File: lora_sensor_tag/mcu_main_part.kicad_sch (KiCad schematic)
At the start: 10 parts, among them U5 ESP32-WROOM-32D, U6 SHT20, U7 SX1276IMLTRT

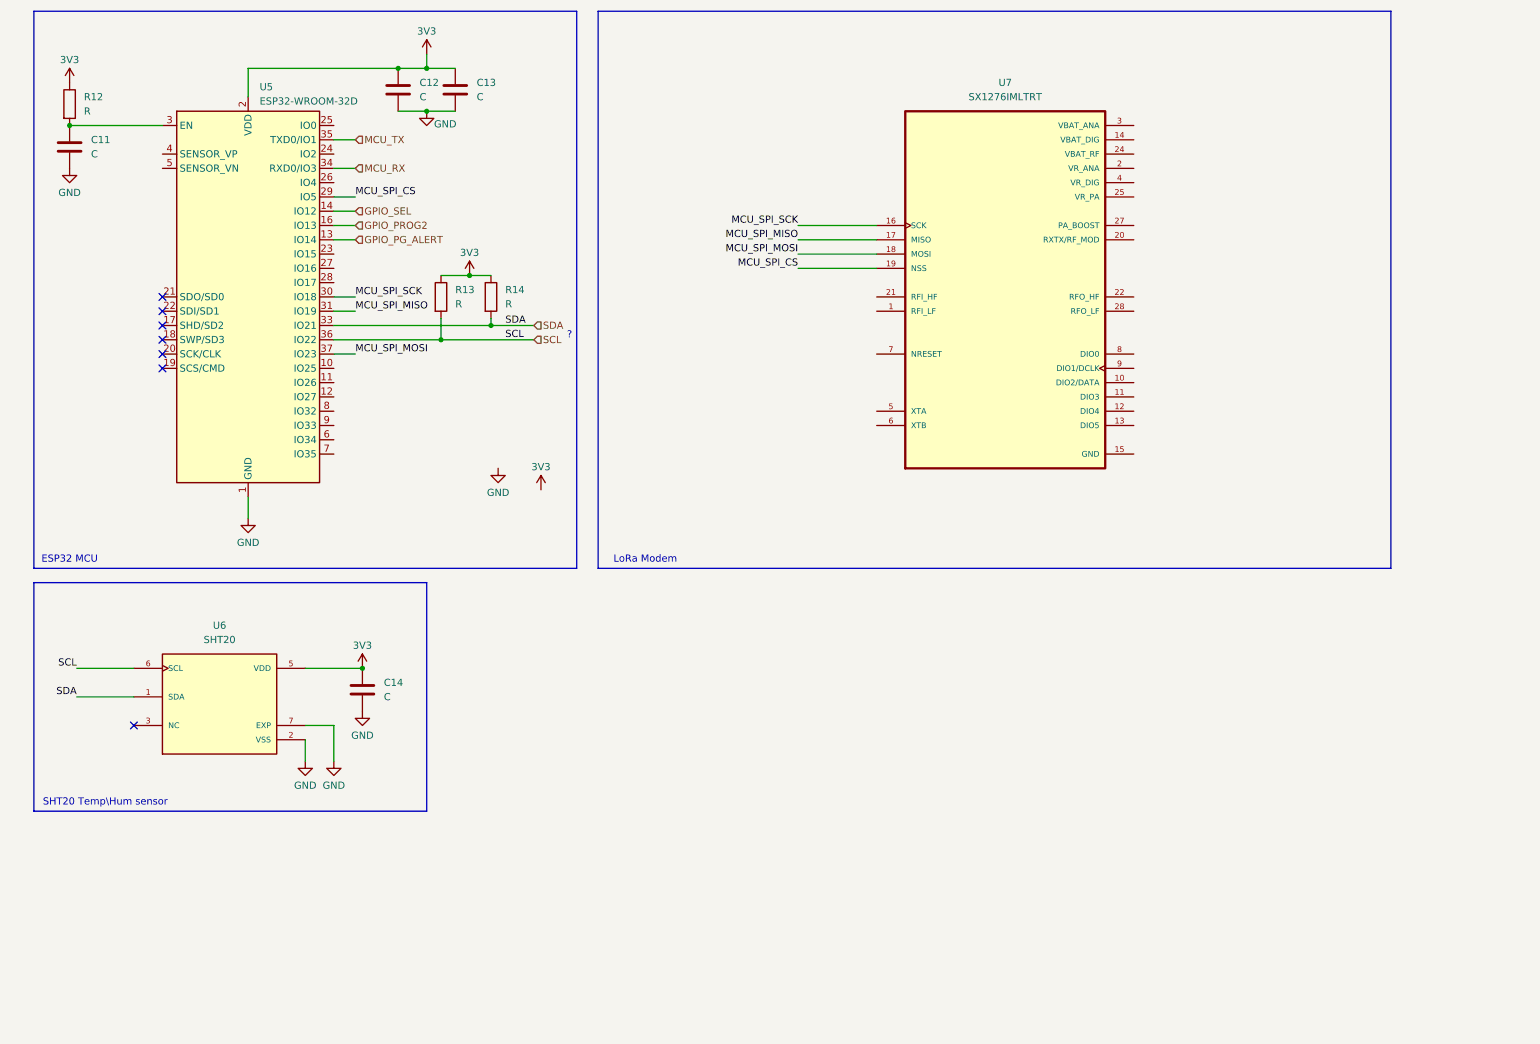
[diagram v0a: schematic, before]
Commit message: lora_sensor_tag: Update shematic
Update schematic with the following changes:
 - Add SX1276 LoRa modem schematic;
 - Add antenna matching network for SX1276 LoRa modem;
 - Add PE4259 RF switch for SX1276 LoRa modem;
 - Add USB-C connector;
 - Add CP2102 USB-to-UART bridge and programming interface;

Signed-off-by: Volodymyr <volodymyrnoha99@gmail.com>
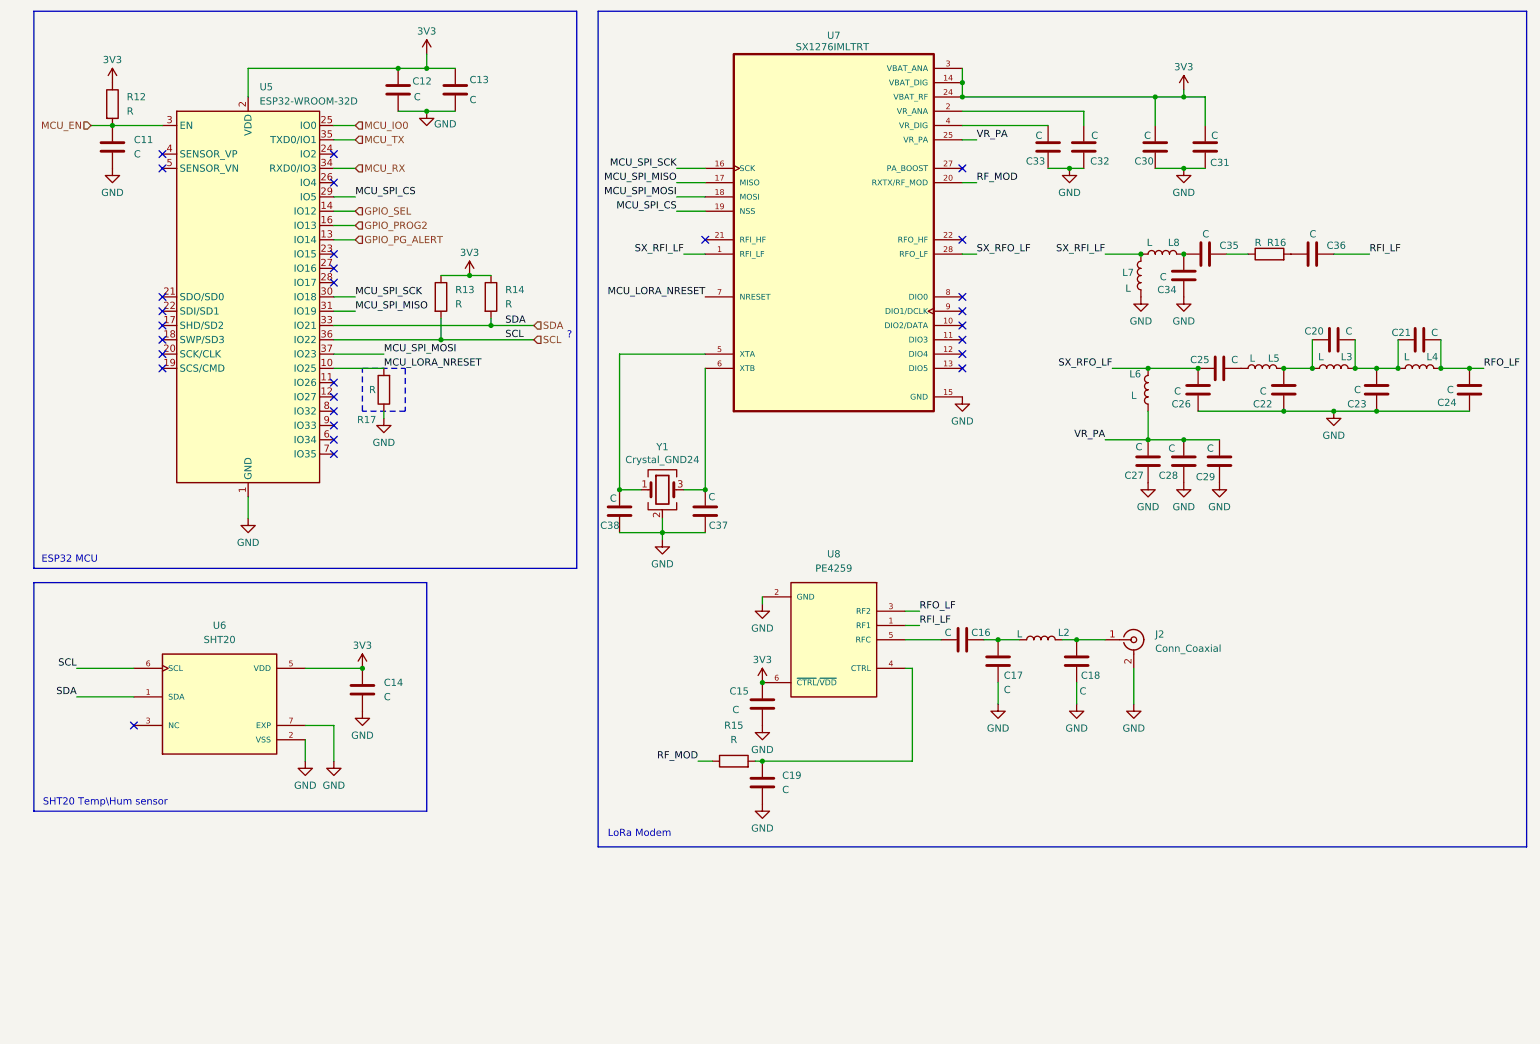
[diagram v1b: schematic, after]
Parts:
- added C15, C16, C17, C18, C19, C20, C21, C22, C23, C24, C25, C26, C27, C28, C29, C30, C31, C32, C33, C34, C35, C36, C37, C38: C, symbol Device:C
- added J2: Conn_Coaxial, Connector_Coaxial:SMA_BAT_Wireless_BWSMA-KWE-Z001, symbol Connector:Conn_Coaxial
- added L2, L3, L4, L5, L6, L7, L8: L, Relay_THT:Relay_DPDT_Finder_30.22, symbol Device:L
- added R15, R16, R17: R, TPS63070RNMR:VREG_TPS63070RNMR, symbol Device:R
- added U8: PE4259, PE4259:SOT65P215X110-6N, symbol PE4259:PE4259
- added Y1: Crystal_GND24, symbol Device:Crystal_GND24
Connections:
- net 3V3: now also U7.14 (VBAT_DIG), U7.24 (VBAT_RF), U7.3 (VBAT_ANA), C15.1, C30.1, C31.1, U8.6 (~{CTRL}/~{VDD})
- net GND: now also C15.2, C17.1, C18.1, C19.1, C22.2, C23.2, C24.2, C26.2, C27.2, C28.2, C29.2, C30.2, C31.2, C32.2, C33.2, C34.2, C37.2, C38.2, J2.2 (Ext), L7.1, R17.1, U8.2 (GND), Y1.2 (G), Y1.4 (G)
- net MCU_EN: now reaches C11.1, R12.2, U5.3 (EN)
- net MCU_LORA_NRESET: now reaches U5.10 (IO25)
- net MCU_LORA_NRESET: now also U7.7 (NRESET), R17.2
- net MCU_IO0: now reaches U5.25 (IO0)
- net SX_RFI_LF: now reaches U7.1 (RFI_LF)
- net SX_RFI_LF: now also L7.2, L8.1
- net at U7.2 (VR_ANA): now also C32.1
- net RF_MOD: now reaches U7.20 (RXTX/RF_MOD)
- net RF_MOD: now also R15.1
- net VR_PA: now reaches U7.25 (VR_PA)
- net VR_PA: now also C27.1, C28.1, C29.1, L6.1
- net SX_RFO_LF: now reaches U7.28 (RFO_LF)
- net SX_RFO_LF: now also C25.2, C26.1, L6.2
- net at U7.4 (VR_DIG): now also C33.1
- net at U7.5 (XTA): now also C38.1, Y1.1
- net at U7.6 (XTB): now also C37.1, Y1.3
- new net: C35.2, R16.1
- new net: C36.1, R16.2
- new net: C25.1, L5.1
- new net: C16.2, C17.2, L2.1
- new net: C18.2, J2.1 (In), L2.2
- new net: C20.1, C21.2, C23.1, L3.2, L4.1
- new net: C16.1, U8.5 (RFC)
- new net: C20.2, C22.1, L3.1, L5.2
- new net: C34.1, C35.1, L8.2
- new net: C19.2, R15.2, U8.4 (CTRL)
- new net RFI_LF: C36.2, U8.1 (RF1)
- new net RFO_LF: C21.1, C24.1, L4.2, U8.3 (RF2)
- no-connect marks 7 -> 29
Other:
- moved on the sheet: C11, R12, U7

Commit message: Update schematic notation and fix bugs
Global labels notation updated;
Swapped line order in schematic fixed;
Added pull-up resistor to PG-ALERT pin (fuel gauge)

Signed-off-by: Volodymyr <volodymyrnoha99@gmail.com>
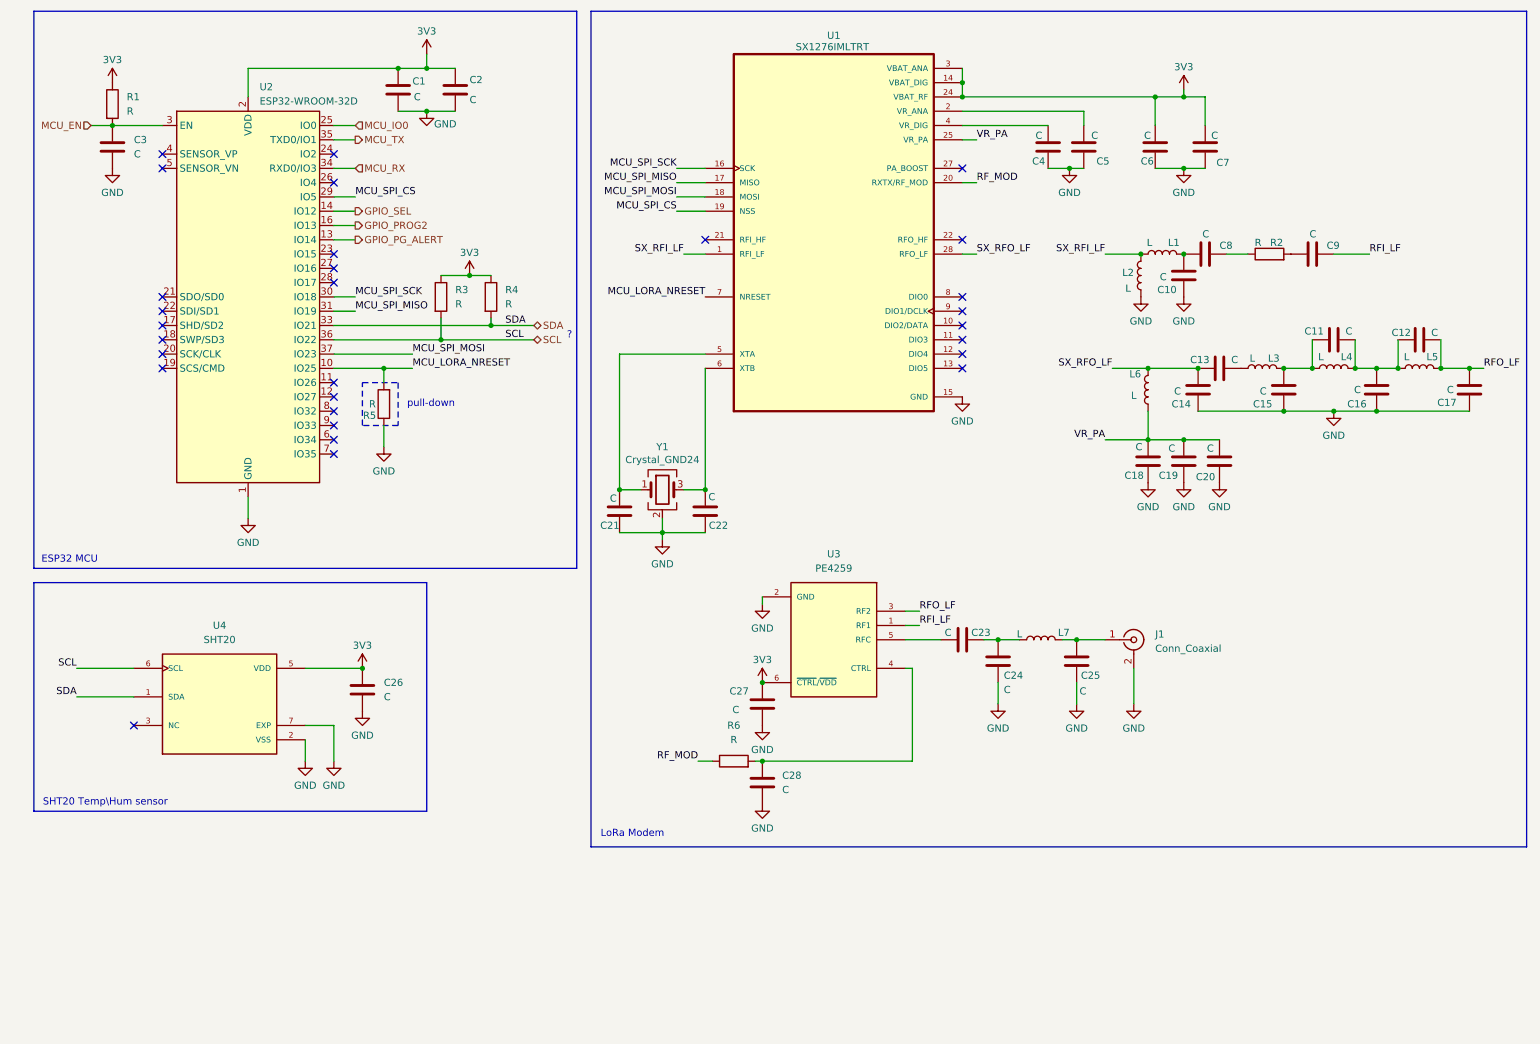
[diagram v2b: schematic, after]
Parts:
- renumbered C12 to C1, C34 to C10, C20 to C11, C21 to C12, C25 to C13, C26 to C14, C22 to C15, C23 to C16, C24 to C17, C27 to C18, C28 to C19, C13 to C2, C29 to C20, C38 to C21, C37 to C22, C16 to C23, C17 to C24, C18 to C25, C14 to C26, C15 to C27, C19 to C28, C11 to C3, C33 to C4, C32 to C5, C30 to C6, C31 to C7, C35 to C8, C36 to C9, J2 to J1, L8 to L1, L7 to L2, L5 to L3, L3 to L4, L4 to L5, L2 to L7, R12 to R1, R16 to R2, R13 to R3, R14 to R4, R17 to R5, R15 to R6, U7 to U1, U5 to U2, U8 to U3, U6 to U4
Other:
- note added: "pull-down"
- title: (none) -> MCU and LoRa main part
- moved on the sheet: R5

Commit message: Bug fixing
The following bugs and issues have been fixed:
- Fixed LoRa Rx\Tx line polarity;
- Removed unnneccessary pull-up\pull-down resistors;
- Added pull-up resistor to IO0;
- Added resistive divider for MCP7387 VPCC pin;
- GPIO_SEL moved from IO4 to IO26 (IO4 used for flash init and can cause unexpected behavior);
- CC1 and CC2 of USB-C port connected to GND via pull-down resistors;

Signed-off-by: Volodymyr <volodymyrnoha99@gmail.com>
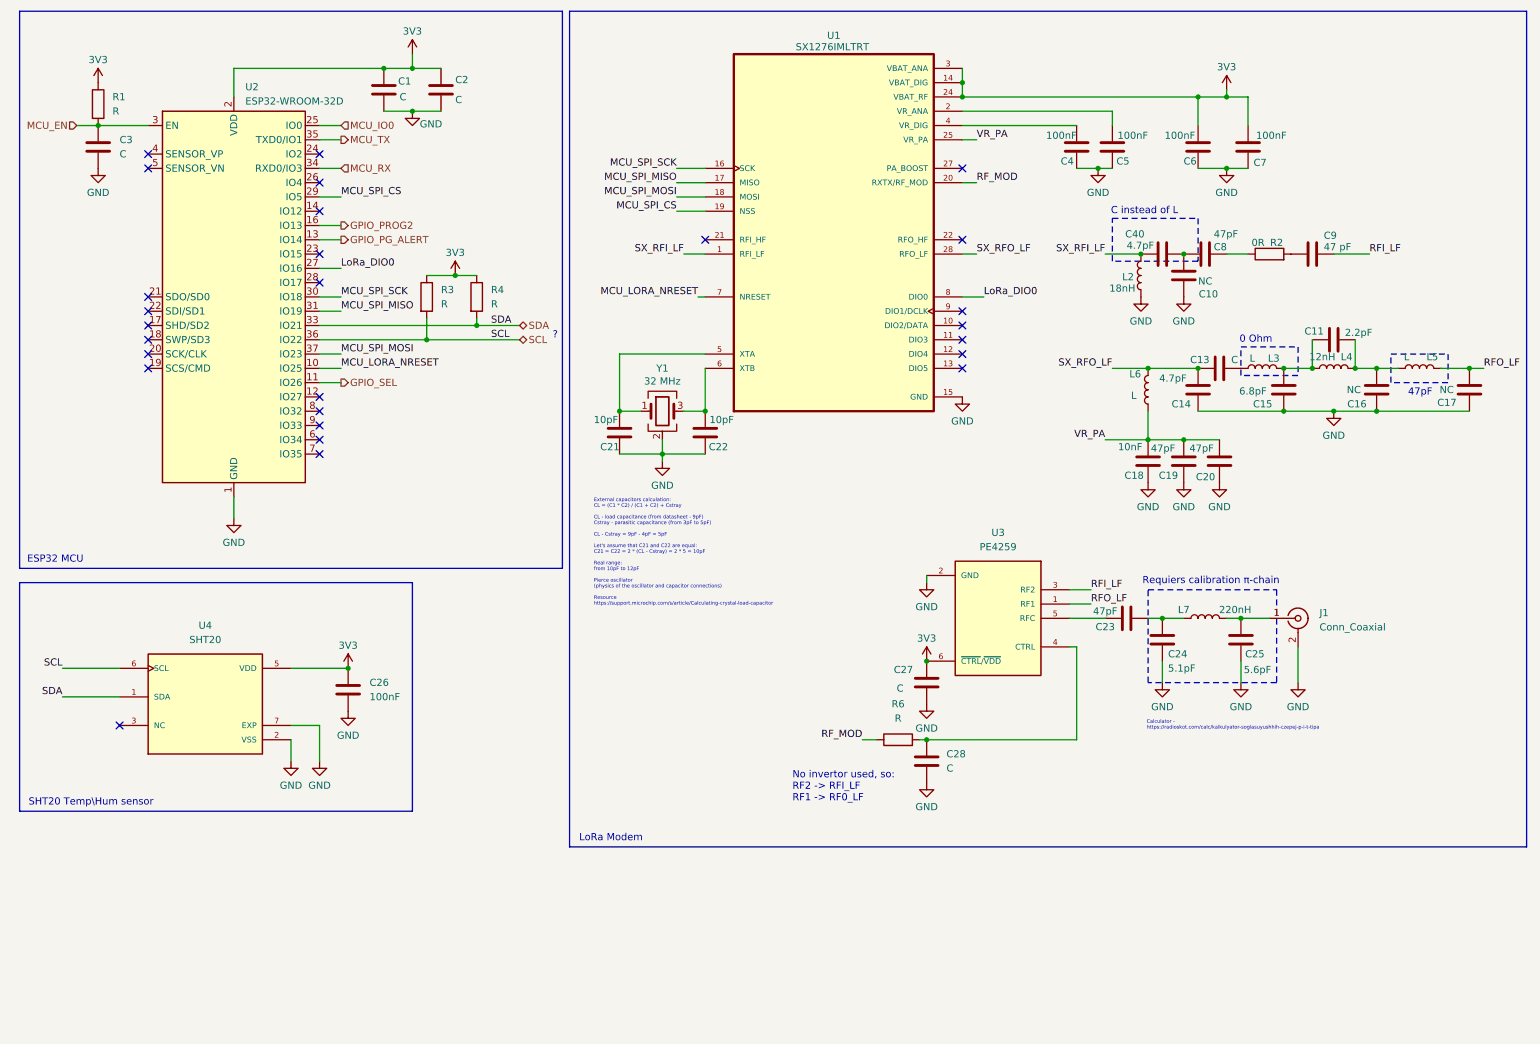
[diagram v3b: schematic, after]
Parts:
- removed C12: C, symbol Device:C
- removed L1: L, Relay_THT:Relay_DPDT_Finder_30.22, symbol Device:L
- removed R5: R, TPS63070RNMR:VREG_TPS63070RNMR, symbol Device:R
- added C40: 4.7pF, symbol Device:C
- C10, C16, C17: value C -> NC
- C11: value C -> 2.2pF
- C14: value C -> 4.7pF
- C15: value C -> 6.8pF
- C18: value C -> 10nF
- C19, C20, C23, C8: value C -> 47pF
- C21, C22: value C -> 10pF
- C24: value C -> 5.1pF
- C25: value C -> 5.6pF
- C26, C4, C5, C6, C7: value C -> 100nF
- C9: value C -> 47 pF
- L2: value L -> 18nH
- L4: value L -> 12nH
- L7: value L -> 220nH
- R2: value R -> 0R
- Y1: value Crystal_GND24 -> 32 MHz
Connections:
- net GPIO_SEL: now also U2.11 (IO26); no longer U2.14 (IO12)
- net RFI_LF: now also U3.3 (RF2); no longer U3.1 (RF1)
- net RFO_LF: now also U3.1 (RF1); no longer U3.3 (RF2)
- net SX_RFI_LF: now also C40.1
- net LoRa_DIO0: now reaches U2.27 (IO16)
- net LoRa_DIO0: now also U1.8 (DIO0)
- net at C10.1, C8.1: now also C40.2
- no-connect marks 29 -> 27
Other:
- note added: "0 Ohm"
- note added: "47pF"
- note added: "C instead of L"
- note added: "Calculator - https://radioskot.com/calc/kalkulyator-soglasuyushhih-czepej-p-i-t-tipa"
- note added: "External capacitors calculation: CL = (C1 * C2) / (C1 + C2) + Cstray CL - load capacitance (from datasheet - 9pF) Cstray - parasitic capacitance (from 3pF to 5pF) CL - Cstray = 9pF - 4pF = 5pF Let's assume that C21 and C22 are equal: C21 = C22 = 2 * (CL - Cstray) = 2 * 5 = 10pF Real range: from 10pF to 12pF Pierce oscillator (physics of the oscillator and capacitor connections) Resource https://s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"
- note added: "No invertor used, so: RF2 -> RFI_LF RF1 -> RF0_LF"
- note added: "Requiers calibration π-chain"
- note removed: "pull-down"
- moved on the sheet: C1, C2, C21, C22, C23, C24, C25, C26, C27, C28, C3, C4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

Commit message: Update Charge Enable mechanism on MCP73871
Adds the following charge enable control mechanism
on MCP73871:

VUSB ──|>|──┐
     D_CE1  │
            ├── V_CE_SRC ── R17 ──┬──── CE, U6.17
VBAT ──|>|──┘             47 кОм  │   |
     D_CE2                        C  R34
                                 │    |
GPIO26 ── R_B ──┬────────────── B Q3 GND
         47 кОм │                │
               R_BE              E   NPN
              100 кОм            │
                │               GND
               GND

This solution allows for controlled enabling of
the charge function  on the MCP73871, ensuring
that the charge enable pin is properly managed
through the diodes and transistor network.The
circuit allows control of the CE pin via the
GPIO26 pin and helps to keep CE in a proper state.

Signed-off-by: Volodymyr <volodymyrnoha99@gmail.com>
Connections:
- net GPIO_CE: now reaches U2.12 (IO27)
- no-connect marks 27 -> 26
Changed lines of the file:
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@@
-	)
-	(no_connect
-		(at 67.31 85.09)
 	)
 	(no_connect
@@
 		(pts
 			(xy 200.66 119.38) (xy 204.47 119.38)
+		)
+		(stroke
+			(width 0)
+			(type default)
+		)
+	)
+	(wire
+		(pts
+			(xy 67.31 85.09) (xy 71.12 85.09)
 		)
 		(stroke
@@
 		(effects
 			(font
+				(size 1.27 1.27)
+			)
+			(justify left)
+		)
+	)
+	(hierarchical_label "GPIO_CE"
+		(shape output)
+		(at 71.12 85.09 0)
+		(effects
+			(font
